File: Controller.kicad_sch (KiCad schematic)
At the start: 20 parts, among them J10 Conn_01x04, J11 Conn_01x03, J12 Conn_01x04_Socket, J13 Conn_01x03, SW4 SW_Omron_B3FS, SW5 SW_Omron_B3FS, SW6 SW_Omron_B3FS

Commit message: rough placement
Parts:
- added R33: 10k, Resistor_SMD:R_0805_2012Metric_Pad1.20x1.40mm_HandSolder, symbol Device:R
- R34, R35, R36, R37, R41: MPN (none) -> RC0805FR-0710KL
- R38: value 4k7 -> 10k; MPN (none) -> RC0805FR-0710KL
- R39: value 4k7 -> 1k; MPN (none) -> RC0805FR-101KL
- R40: value 2k -> 1k; MPN (none) -> RC0805FR-101KL
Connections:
- net +5V: now also R33.2; no longer R39.2
- net GND: now also R40.2; no longer R40.1
- net SCL: now also R33.1; no longer R38.1
- net SDA: now also R38.1; no longer R39.1
- net at A1.6 (D3), R37.1: now also R39.1; no longer R40.2
- new net: R39.2, R40.1

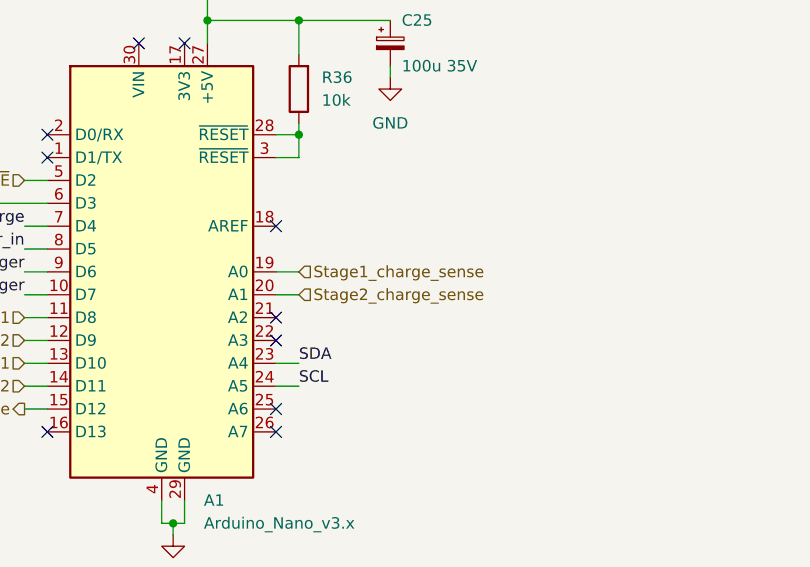
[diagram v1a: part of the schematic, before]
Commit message: firing routing, uC routing done
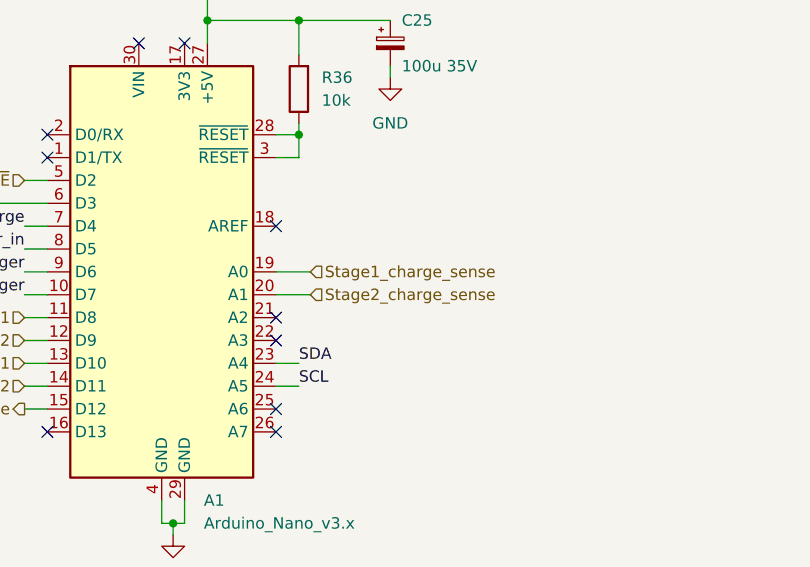
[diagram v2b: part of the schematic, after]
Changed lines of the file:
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@@
+	(wire
+		(pts
+			(xy 151.13 78.74) (xy 154.94 78.74)
+		)
+		(stroke
+			(width 0)
+			(type default)
+		)
+	)
 	(wire
 		(pts
@@
 	(wire
 		(pts
-			(xy 151.13 78.74) (xy 153.67 78.74)
-		)
-		(stroke
-			(width 0)
-			(type default)
-		)
-	)
-	(wire
-		(pts
 			(xy 254 72.39) (xy 254 85.09)
 		)
@@
 	(wire
 		(pts
+			(xy 151.13 81.28) (xy 154.94 81.28)
+		)
+		(stroke
+			(width 0)
+			(type default)
+		)
+	)
+	(wire
+		(pts
 			(xy 271.78 140.97) (xy 271.78 139.7)
 		)
@@
 		(pts
 			(xy 167.64 143.51) (xy 176.53 143.51)
-		)
-		(stroke
-			(width 0)
-			(type default)
-		)
-	)
-	(wire
-		(pts
-			(xy 151.13 81.28) (xy 153.67 81.28)
 		)
 		(stroke
@@
 	(hierarchical_label "Stage1_charge_sense"
 		(shape input)
-		(at 153.67 78.74 0)
+		(at 154.94 78.74 0)
 		(effects
 			(font
@@
 	(hierarchical_label "Stage2_charge_sense"
 		(shape input)
-		(at 153.67 81.28 0)
-		(effects
-			(font
+		(at 154.94 81.28 0)
+		(effects
+			(font

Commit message: update fab files ;/
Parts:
- A1, J10, J11, J12, J13: now not fitted
- C25: LCSC_Part_# (none) -> C109392
- R33, R34, R35, R36, R37, R38, R41: LCSC_Part_# (none) -> C84376
- R39, R40: LCSC_Part_# (none) -> C5842544
- SW4, SW5, SW6: LCSC_Part_# (none) -> C93157
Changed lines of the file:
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@@
+			)
+		)
+		(property "LCSC_Part_#" "C84376"
+			(at 90.17 66.04 0)
+			(effects
+				(font
+					(size 1.27 1.27)
+				)
+				(hide yes)
 			)
 		)
@@
 		)
 		(property "MPN" "B3F-1000"
+			(at 261.62 67.31 0)
+			(effects
+				(font
+					(size 1.27 1.27)
+				)
+				(hide yes)
+			)
+		)
+		(property "LCSC_Part_#" "C93157"
 			(at 261.62 67.31 0)
 			(effects
@@
 			)
 		)
+		(property "LCSC_Part_#" "C84376"
+			(at 257.81 158.75 0)
+			(effects
+				(font
+					(size 1.27 1.27)
+				)
+				(hide yes)
+			)
+		)
 		(pin "2"
 		)
@@
 		(in_bom yes)
 		(on_board yes)
-		(dnp no)
+		(dnp yes)
 		(property "Reference" "J10"
 			(at 222.25 113.03 90)
@@
 			)
 		)
+		(property "LCSC_Part_#" ""
+			(at 228.6 110.49 90)
+			(effects
+				(font
+					(size 1.27 1.27)
+				)
+				(hide yes)
+			)
+		)
 		(pin "3"
 		)
@@
 		(in_bom yes)
 		(on_board yes)
-		(dnp no)
+		(dnp yes)
 		(fields_autoplaced yes)
 		(property "Reference" "A1"
@@
 			)
 		)
+		(property "LCSC_Part_#" ""
+			(at 138.43 78.74 0)
+			(effects
+				(font
+					(size 1.27 1.27)
+				)
+				(hide yes)
+			)
+		)
 		(pin "15"
 		)
@@
 			)
 		)
+		(property "LCSC_Part_#" "C84376"
+			(at 180.34 143.51 90)
+			(effects
+				(font
+					(size 1.27 1.27)
+				)
+				(hide yes)
+			)
+		)
 		(pin "2"
 		)
@@
 			)
 		)
+		(property "LCSC_Part_#" ""
+			(at 266.7 123.19 90)
+			(effects
+				(font
+					(size 1.27 1.27)
+				)
+				(hide yes)
+			)
+		)
 		(pin "1"
 		)
@@
 		)
 		(property "MPN" "151051RS11000"
+			(at 266.7 158.75 90)
+			(effects
+				(font
+					(size 1.27 1.27)
+				)
+				(hide yes)
+			)
+		)
+		(property "LCSC_Part_#" ""
 			(at 266.7 158.75 90)
 			(effects
@@
 			)
 		)
+		(property "LCSC_Part_#" "C84376"
+			(at 257.81 123.19 0)
+			(effects
+				(font
+					(size 1.27 1.27)
+				)
+				(hide yes)
+			)
+		)
 		(pin "2"
 		)
@@
 			)
 		)
+		(property "LCSC_Part_#" "C5842544"
+			(at 90.17 77.47 0)
+			(effects
+				(font
+					(size 1.27 1.27)
+				)
+				(hide yes)
+			)
+		)
 		(pin "2"
 		)
@@
 		(in_bom yes)
 		(on_board yes)
-		(dnp no)
+		(dnp yes)
 		(property "Reference" "J11"
 			(at 222.25 149.86 90)
@@
 		(property "Description" "Generic connector, single row, 01x03, script generated (kicad-library-utils/schlib/autogen/connector/)"
 			(at 228.6 146.05 0)
+			(effects
+				(font
+					(size 1.27 1.27)
+				)
+				(hide yes)
+			)
+		)
+		(property "LCSC_Part_#" ""
+			(at 228.6 146.05 90)
 			(effects
 				(font
@@
 			)
 		)
+		(property "LCSC_Part_#" "C84376"
+			(at 257.81 85.09 0)
+			(effects
+				(font
+					(size 1.27 1.27)
+				)
+				(hide yes)
+			)
+		)
 		(pin "2"
 		)
@@
 		)
 		(property "MPN" "RC0805FR-0710KL"
+			(at 173.99 140.97 90)
+			(effects
+				(font
+					(size 1.27 1.27)
+				)
+				(hide yes)
+			)
+		)
+		(property "LCSC_Part_#" "C84376"
 			(at 173.99 140.97 90)
 			(effects
@@
 			)
 		)
+		(property "LCSC_Part_#" "C93157"
+			(at 261.62 140.97 0)
+			(effects
+				(font
+					(size 1.27 1.27)
+				)
+				(hide yes)
+			)
+		)
 		(pin "1"
 		)
@@
 			)
 		)
+		(property "LCSC_Part_#" "C84376"
+			(at 153.67 58.42 0)
+			(effects
+				(font
+					(size 1.27 1.27)
+				)
+				(hide yes)
+			)
+		)
 		(pin "2"
 		)
@@
 			)
 		)
+		(property "LCSC_Part_#" ""
+			(at 266.7 85.09 90)
+			(effects
+				(font
+					(size 1.27 1.27)
+				)
+				(hide yes)
+			)
+		)
 		(pin "1"
 		)
@@
 			)
 		)
+		(property "LCSC_Part_#" "C93157"
+			(at 256.54 105.41 0)
+			(effects
+				(font
+					(size 1.27 1.27)
+				)
+				(hide yes)
+			)
+		)
 		(pin "1"
 		)
@@
 		(in_bom yes)
 		(on_board yes)
-		(dnp no)
+		(dnp yes)
 		(property "Reference" "J13"
 			(at 222.25 76.2 90)
@@
 			)
 		)
+		(property "LCSC_Part_#" ""
+			(at 228.6 72.39 90)
+			(effects
+				(font
+					(size 1.27 1.27)
+				)
+				(hide yes)
+			)
+		)
 		(pin "2"
 		)
@@
 		(in_bom yes)
 		(on_board yes)
-		(dnp no)
+		(dnp yes)
 		(property "Reference" "J12"
 			(at 196.85 143.5099 0)
@@
 			)
 		)
+		(property "LCSC_Part_#" ""
+			(at 195.58 143.51 0)
+			(effects
+				(font
+					(size 1.27 1.27)
+				)
+				(hide yes)
+			)
+		)
 		(pin "4"
 		)
@@
 			)
 		)
+		(property "LCSC_Part_#" "C5842544"
+			(at 90.17 86.36 0)
+			(effects
+				(font
+					(size 1.27 1.27)
+				)
+				(hide yes)
+			)
+		)
 		(pin "2"
 		)
@@
 			(at 163.83 53.34 0)
 			(effects
+				(font
+					(size 1.27 1.27)
+				)
+				(hide yes)
+			)
+		)
+		(property "LCSC_Part_#" "C109392"
+			(at 163.83 53.34 0)
+			(effects
